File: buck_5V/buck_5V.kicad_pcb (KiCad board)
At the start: 2 copper layers, 11 parts, among them U901 MT2499A

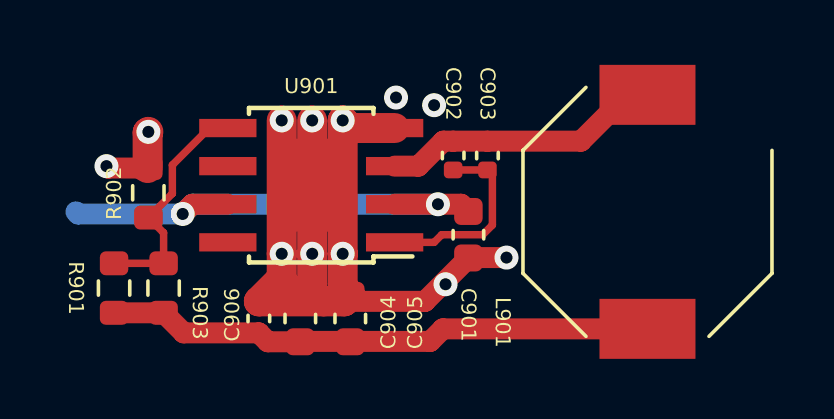
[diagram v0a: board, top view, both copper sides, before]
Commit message: removed hierarchial labels for power symbols and replaced them with actual power symbols also updated footprint of the inductor of the 5V buck
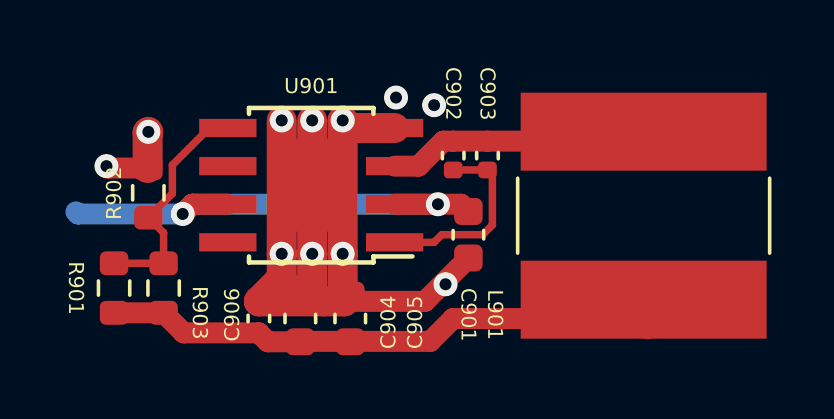
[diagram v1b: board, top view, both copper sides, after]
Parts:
- L901: footprint Inductor_SMD:L_Bourns-SRU8028_8.0x8.0mm -> Inductor_SMD:L_Bourns-SRN8040_8x8.15mm
- moved L901 0.18 mm to (100.1, 96.5)
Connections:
- net /5V renamed +5V
- net /GND renamed GND
- net /VDC_in renamed VCC
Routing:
- net Net-(U901-SW): track 9.41 -> 6.56 mm
- net GND: track 32.6 -> 31.3 mm, vias 12 -> 11
